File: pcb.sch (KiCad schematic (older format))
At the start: 0 parts

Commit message: trying commits work out
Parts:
- added D?: LED, symbol device:LED
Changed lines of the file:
@@
 Comment4 ""
 $EndDescr
+$Comp
+L device:LED D?
+U 1 1 620EFBAD
+P 5050 4850
+F 0 "D?" H 5043 5066 50  0000 C CNN
+F 1 "LED" H 5043 4975 50  0000 C CNN
+F 2 "" H 5050 4850 50  0001 C CNN
+F 3 "~" H 5050 4850 50  0001 C CNN
+	1    5050 4850
+	1    0    0    -1
+$EndComp
 $EndSCHEMATC

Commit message: triying second commit
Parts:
- removed D?: LED, symbol device:LED
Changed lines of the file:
@@
 Comment4 ""
 $EndDescr
-$Comp
-L device:LED D?
-U 1 1 620EFBAD
-P 5050 4850
-F 0 "D?" H 5043 5066 50  0000 C CNN
-F 1 "LED" H 5043 4975 50  0000 C CNN
-F 2 "" H 5050 4850 50  0001 C CNN
-F 3 "~" H 5050 4850 50  0001 C CNN
-	1    5050 4850
-	1    0    0    -1
-$EndComp
 $EndSCHEMATC

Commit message: Added led to schematic
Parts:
- added D?: LED, symbol device:LED
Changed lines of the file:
@@
 Comment4 ""
 $EndDescr
+$Comp
+L device:LED D?
+U 1 1 620F14A9
+P 5250 4100
+F 0 "D?" H 5243 4316 50  0000 C CNN
+F 1 "LED" H 5243 4225 50  0000 C CNN
+F 2 "" H 5250 4100 50  0001 C CNN
+F 3 "~" H 5250 4100 50  0001 C CNN
+	1    5250 4100
+	1    0    0    -1
+$EndComp
 $EndSCHEMATC

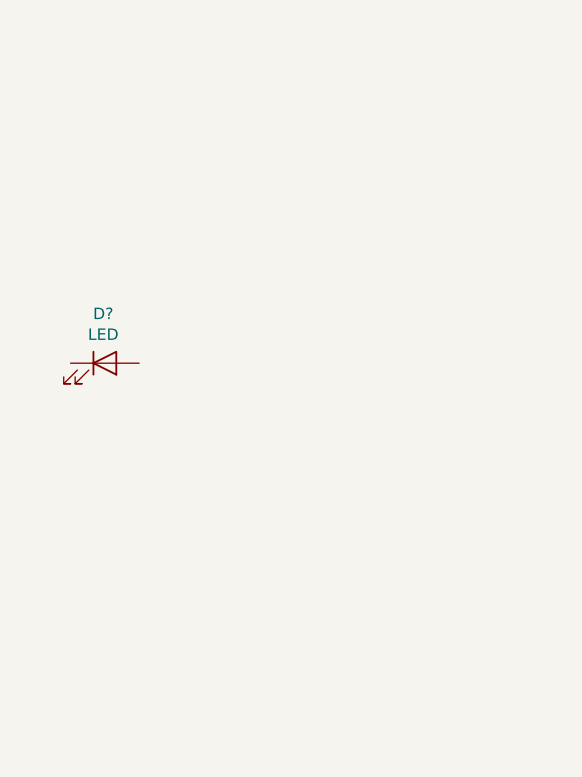
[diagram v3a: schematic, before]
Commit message: added microcontroller to schematic
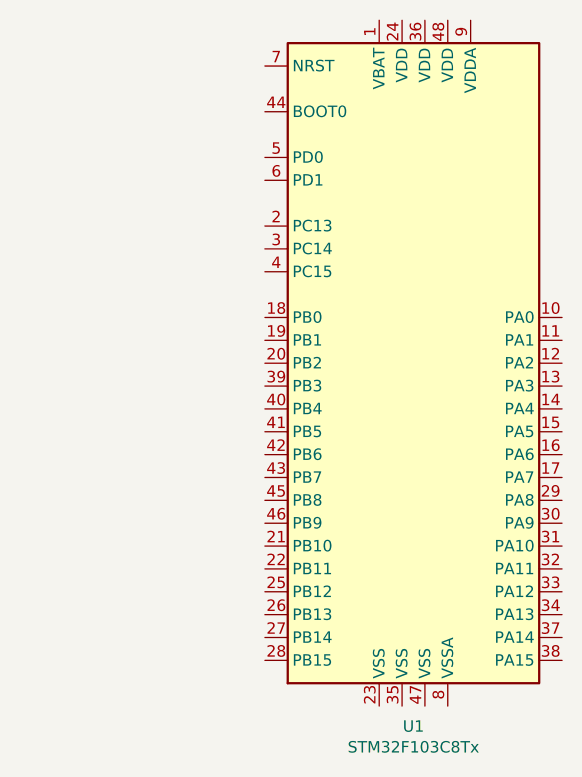
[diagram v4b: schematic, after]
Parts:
- removed D?: LED, symbol device:LED
- added U1: STM32F103C8Tx, Package_QFP:LQFP-48_7x7mm_P0.5mm, symbol MCU_ST_STM32F1:STM32F103C8Tx
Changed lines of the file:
@@
 $EndDescr
 $Comp
-L device:LED D?
-U 1 1 620F14A9
-P 5250 4100
-F 0 "D?" H 5243 4316 50  0000 C CNN
-F 1 "LED" H 5243 4225 50  0000 C CNN
-F 2 "" H 5250 4100 50  0001 C CNN
-F 3 "~" H 5250 4100 50  0001 C CNN
-	1    5250 4100
+L MCU_ST_STM32F1:STM32F103C8Tx U1
+U 1 1 620F1E41
+P 6650 4100
+F 0 "U1" H 6600 2511 50  0000 C CNN
+F 1 "STM32F103C8Tx" H 6600 2420 50  0000 C CNN
+F 2 "Package_QFP:LQFP-48_7x7mm_P0.5mm" H 6050 2700 50  0001 R CNN
+F 3 "http://www.st.com/st-web-ui/static/active/en/resource/technical/document/datasheet/CD00161566.pdf" H 6650 4100 50  0001 C CNN
+	1    6650 4100
 	1    0    0    -1
 $EndComp
